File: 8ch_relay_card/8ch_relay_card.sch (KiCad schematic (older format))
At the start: 59 parts, among them J1 CamdenBoss CTB3051/10BK, J10 jmp_3way, J11 TruConnect XY-305, J12 TruConnect XY-305, J13 TruConnect XY-305, J14 TruConnect XY-305, J15 TruConnect XY-305, J16 TruConnect XY-305, J17 TruConnect XY-305, J18 TruConnect XY-305, J2 jmp_3way, J20 TruConnect 21-3000, J3 jmp_3way, J4 jmp_3way, J5 jmp_3way, J6 jmp_3way, J7 jmp_3way, J8 jmp_3way, J9 jmp_3way, Q17 STD12NF06L, U1 ULN2803

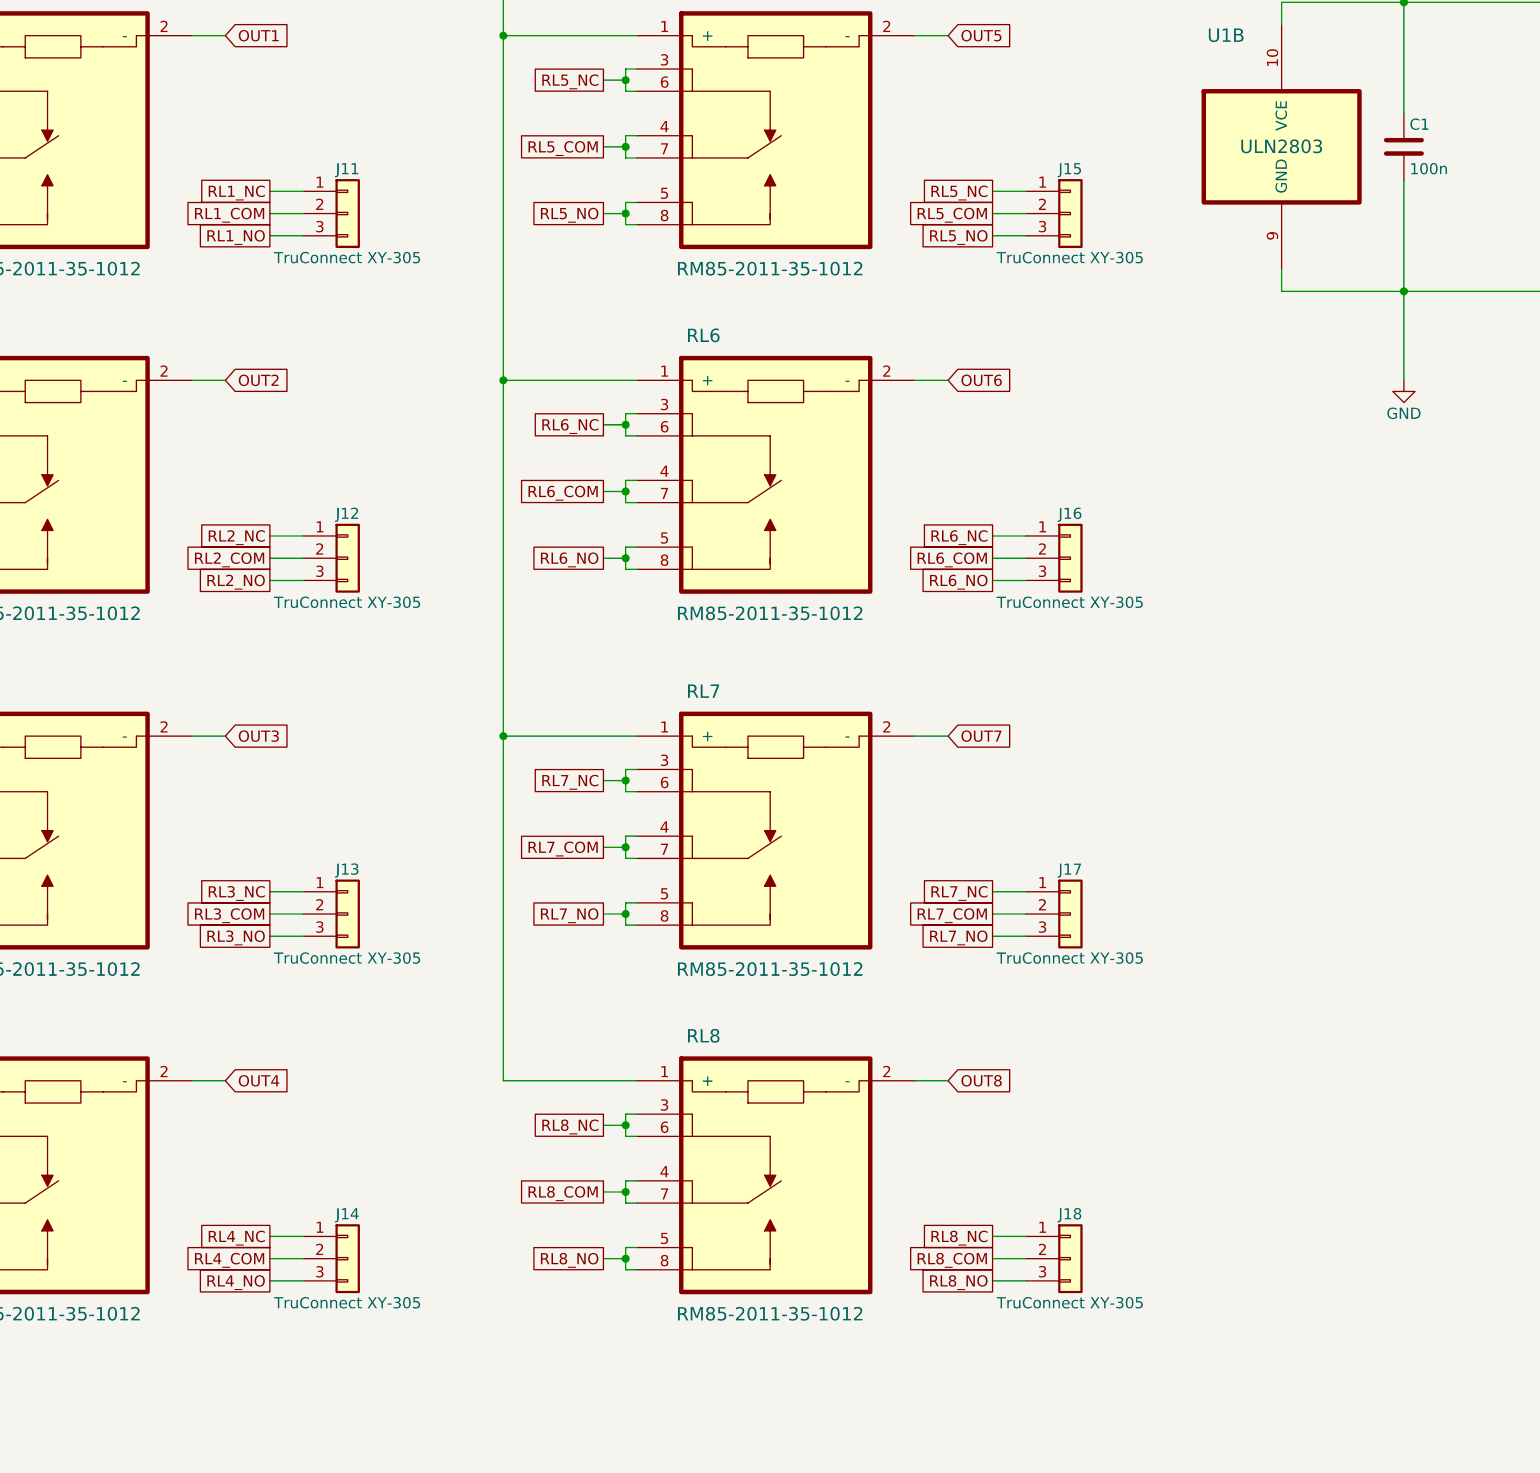
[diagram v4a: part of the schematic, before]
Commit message: V1.1: Changed relay layout to improve solderability, especially on home-made PCBs without through-plating. Changed output connector to a all-in-one stacked version
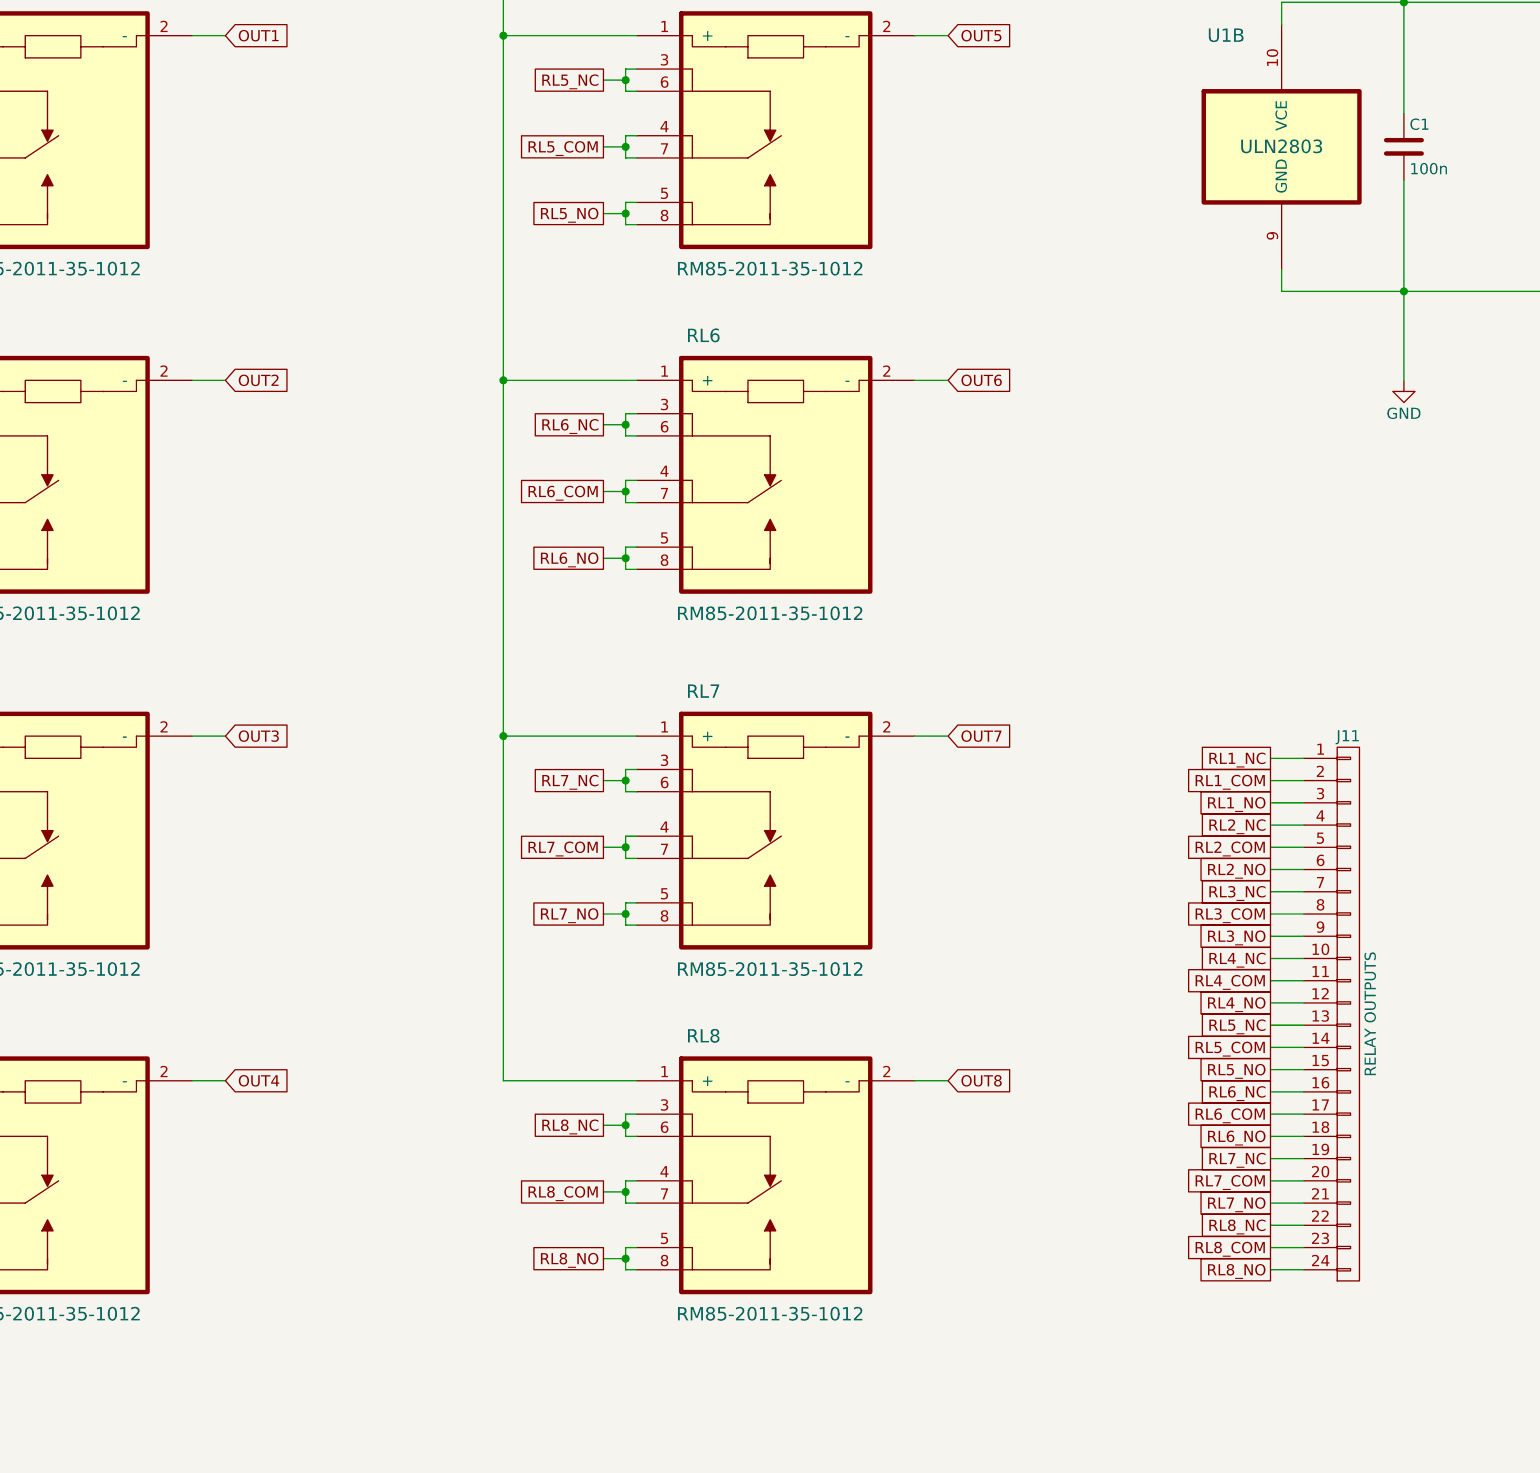
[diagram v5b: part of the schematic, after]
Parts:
- removed J11, J12, J13, J14, J15, J16, J17, J18: TruConnect XY-305, bjh-kicad-connector-fp:TruConnect_21-1812, symbol Conn_01x03
- added J11: RELAY OUTPUTS, bjh-kicad-connector-fp:TruConnect_21-1812_x8_stacked, symbol CONN_01X24
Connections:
- net RL1_COM: now also J11.2 (P2)
- net RL1_NC: now also J11.1 (P1)
- net RL1_NO: now also J11.3 (P3)
- net RL2_COM: now also J11.5 (P5)
- net RL2_NC: now also J11.4 (P4)
- net RL2_NO: now also J11.6 (P6)
- net RL3_COM: now also J11.8 (P8)
- net RL3_NC: now also J11.7 (P7)
- net RL3_NO: now also J11.9 (P9)
- net RL4_COM: now also J11.11 (P11)
- net RL4_NC: now also J11.10 (P10)
- net RL4_NO: now also J11.12 (P12)
- net RL5_COM: now also J11.14 (P14)
- net RL5_NC: now also J11.13 (P13)
- net RL5_NO: now also J11.15 (P15)
- net RL6_COM: now also J11.17 (P17)
- net RL6_NC: now also J11.16 (P16)
- net RL6_NO: now also J11.18 (P18)
- net RL7_COM: now also J11.20 (P20)
- net RL7_NC: now also J11.19 (P19)
- net RL7_NO: now also J11.21 (P21)
- net RL8_COM: now also J11.23 (P23)
- net RL8_NC: now also J11.22 (P22)
- net RL8_NO: now also J11.24 (P24)
